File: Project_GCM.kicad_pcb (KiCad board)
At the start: 4 copper layers, 203 x 116 mm, 127 parts, among them J1 Molex_1053102116, J10 MM1_addressExtension, J11 MM1_receptacle_5530843-2, J12 DEBUG_BUSES, J13 MM1_addressExtension, J2 PP1_receptacle_TE_5-5530843-4, J3 PP1_receptacle_TE_5-5530843-4, J4 PP1_receptacle_TE_5-5530843-4, J5 PP1_receptacle_TE_5-5530843-4, J6 TE_Eurocard_96pole, J7 3-641124-6, J8 MM1_receptacle_5530843-2, J9 Conn_01x02, U1 LM810, U10 74LVC1G74, U11 74AHC1G04, U12 74AHC244, U13 CD74AC161M, U14 CD74AC161M, U15 74AHCT1G04, U16 CD74AC161M, U17 CD74AC161M, U18 74AHC1G04, U19 CD74AC161M, U2 LTC6994xS6-1, U20 CD74AC161M, U21 74AHCT244, U22 74CBTLV16212, U23 74CBTLV16212, U24 74CBTLV16212, U25 74AHC1G32, U26 SN74LV393A, U27 SN74LV393A, U28 CD74AC151, U29 CD74AC151, U3 74AHC1G32, U30 74AHC1G32, U31 CD74AC151, U32 74AHC273, U33 SN74LV393A, U34 SN74LV393A, U35 CD74AC151, U36 CD74AC151, U37 CD74AC151, U4 74AHC273, U40 74AHC273, U41 74AHC1G04, U42 74AHC273, U43 74AHC273, U44 74AHC273, U5 74AHC1G04, U6 CD74AC238, U7 74AHC138, U8 74AHC244, U9 74AHC244, X1 ECS-2200BX-500

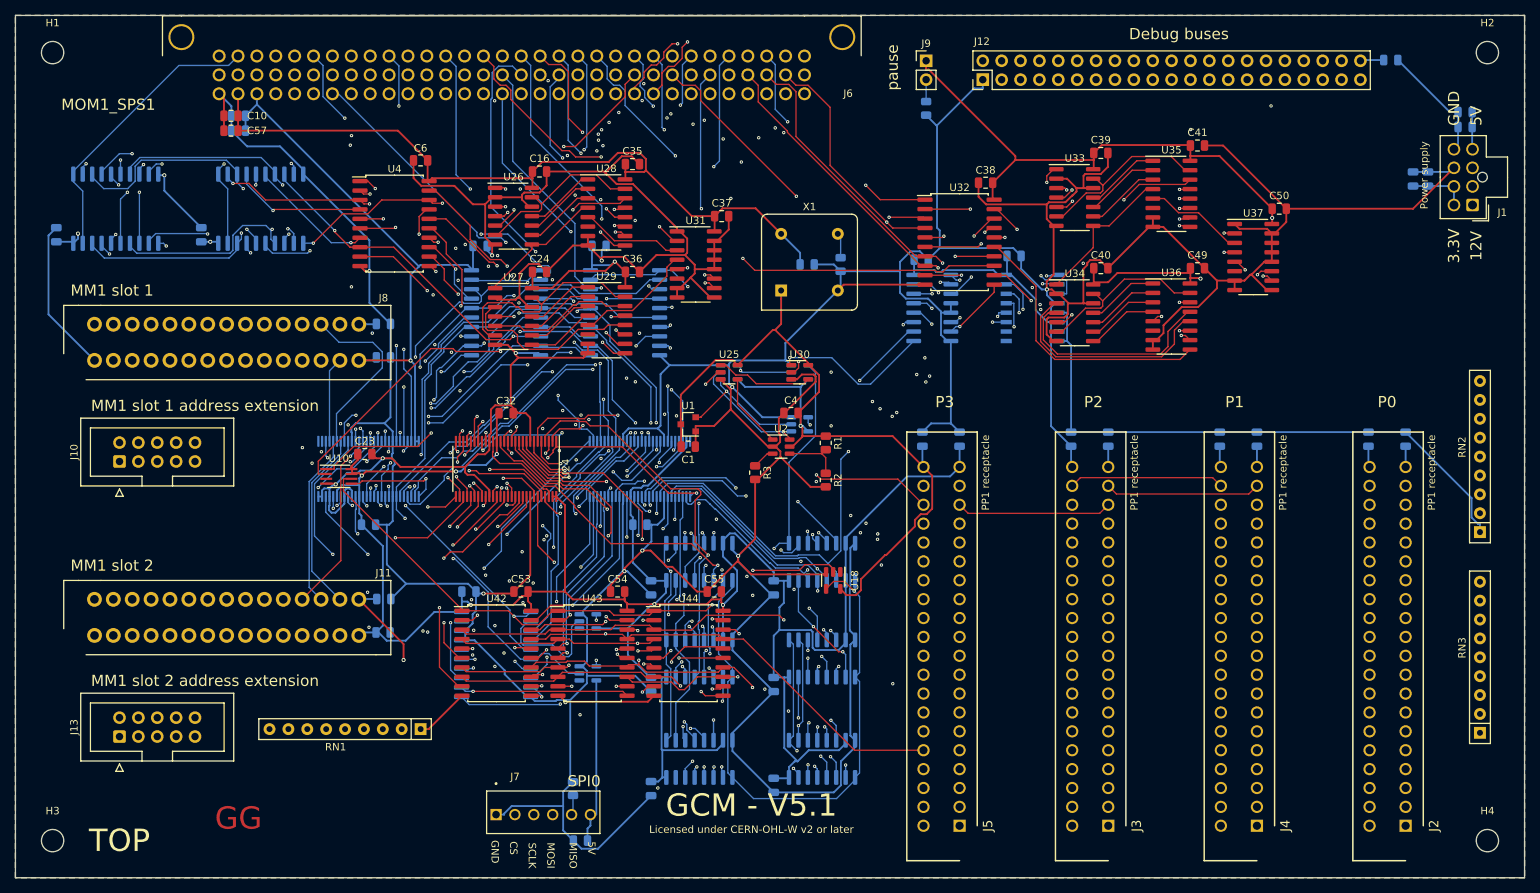
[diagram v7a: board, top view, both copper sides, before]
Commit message: Clean bottom layer
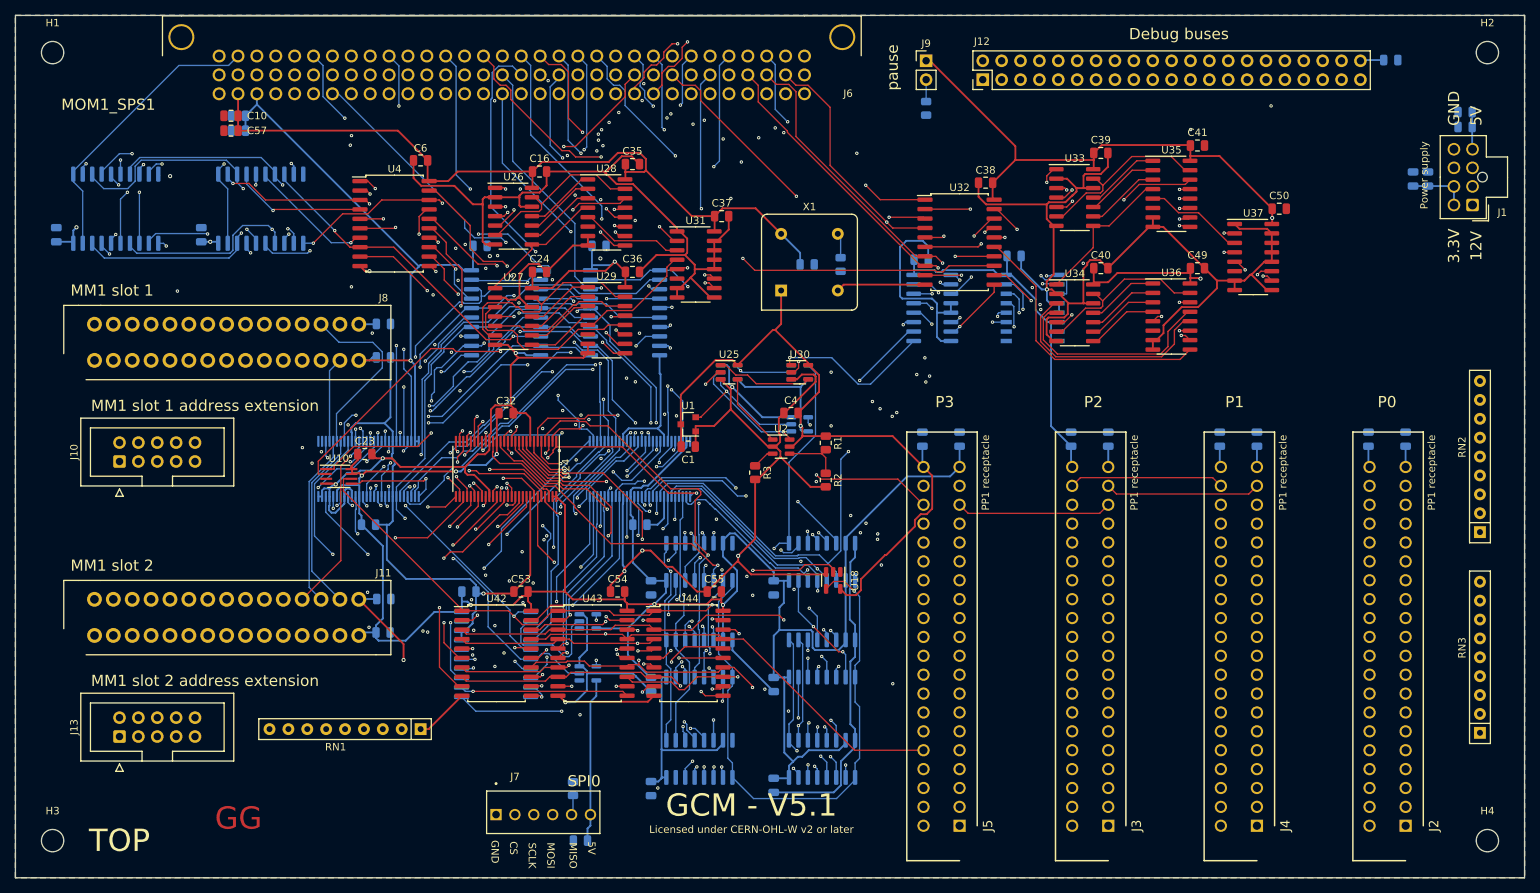
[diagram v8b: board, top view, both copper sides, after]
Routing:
- net GND: track 1410.1 -> 792.5 mm, vias 14 -> 16
- net +5V: track 755.6 -> 756.8 mm
- net +3V3: track 540.7 -> 541.5 mm
- net /ClockGenerator/CLK_SELECT_1: track 44.9 -> 45.6 mm
- net /Connector/BREAD2_7: track 253.4 -> 254.0 mm
- net /Connector/BREAD2_4: track 241.7 -> 242.3 mm
